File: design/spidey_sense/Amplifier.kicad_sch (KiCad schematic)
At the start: 5 parts, among them U6 LT1001

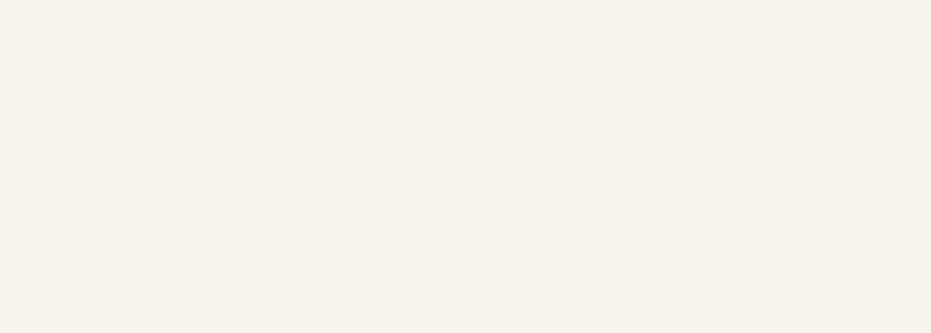
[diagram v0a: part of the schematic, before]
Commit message: Added vias to avoid GND loops
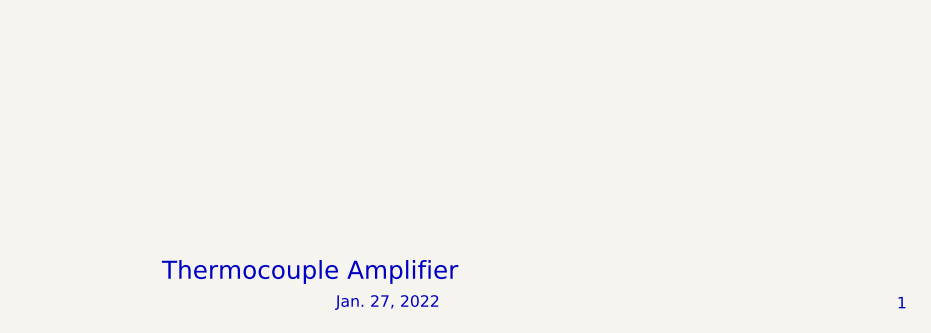
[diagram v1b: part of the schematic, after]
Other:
- note added: "1"
- note added: "Jan. 27, 2022"
- note added: "Thermocouple Amplifier"
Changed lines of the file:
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@@
     (stroke (width 0) (type default) (color 0 0 0 0))
+  )
+  (text "Thermocouple Amplifier" (at 186.6841 190.9188 0)
+    (effects (font (size 2 2)) (justify left bottom))
   )
   (text "R3*0.99 > 17.1k" (at 163.83 99.06 0)
@@
     (effects (font (size 1.27 1.27)) (justify left bottom))
   )
+  (text "1" (at 268.3346 194.1105 0)
+    (effects (font (size 1.27 1.27)) (justify left bottom))
+  )
+  (text "Jan. 27, 2022" (at 206.0014 193.9392 0)
+    (effects (font (size 1.27 1.27)) (justify left bottom))
+  )

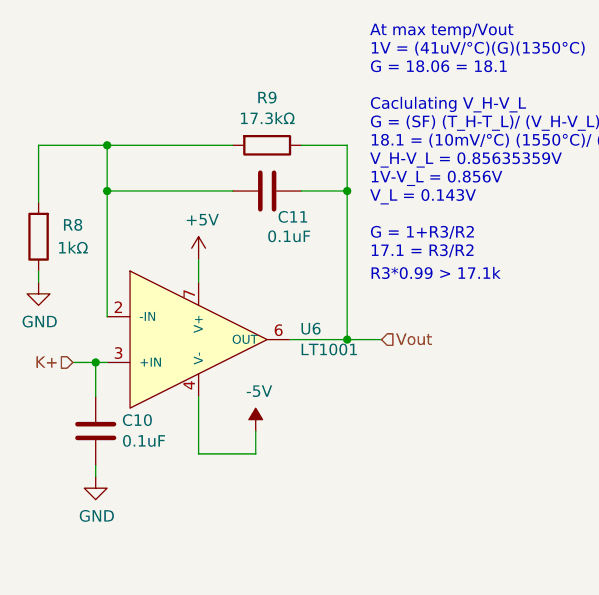
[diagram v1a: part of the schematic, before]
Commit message: Changed C5 value
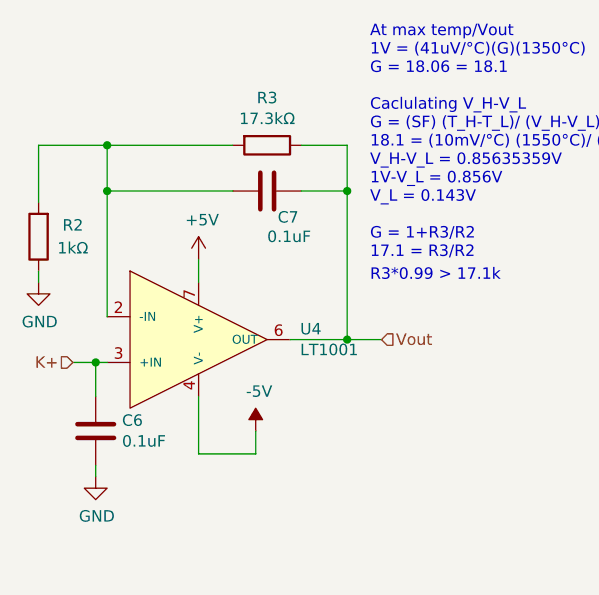
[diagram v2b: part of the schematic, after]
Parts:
- renumbered C10 to C6, C11 to C7, R8 to R2, R9 to R3, U6 to U4
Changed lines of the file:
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@@
   (symbol (lib_id "Device:R") (at 127 93.98 180)
     (in_bom yes) (on_board yes)
-    (property "Reference" "R8" (id 0) (at 130.81 92.71 0))
+    (property "Reference" "R2" (id 0) (at 130.81 92.71 0))
     (property "Value" "1kΩ" (id 1) (at 130.81 95.25 0))
     (property "Footprint" "Resistor_SMD:R_0805_2012Metric_Pad1.20x1.40mm_HandSolder" (id 2) (at 128.778 93.98 90)
@@
   (symbol (lib_id "Device:C") (at 133.35 115.57 0)
     (in_bom yes) (on_board yes)
-    (property "Reference" "C10" (id 0) (at 136.271 114.4016 0)
+    (property "Reference" "C6" (id 0) (at 136.271 114.4016 0)
       (effects (font (size 1.27 1.27)) (justify left))
     )
@@
   (symbol (lib_id "Device:C") (at 152.4 88.9 270)
     (in_bom yes) (on_board yes)
-    (property "Reference" "C11" (id 0) (at 153.5684 91.821 90)
+    (property "Reference" "C7" (id 0) (at 153.5684 91.821 90)
       (effects (font (size 1.27 1.27)) (justify left))
     )
@@
   (symbol (lib_id "power:GND") (at 133.35 120.65 0)
     (in_bom yes) (on_board yes)
-    (property "Reference" "#PWR026" (id 0) (at 133.35 127 0)
+    (property "Reference" "#PWR022" (id 0) (at 133.35 127 0)
       (effects (font (size 1.27 1.27)) hide)
     )
@@
   (symbol (lib_id "power:GND") (at 127 99.06 0)
     (in_bom yes) (on_board yes)
-    (property "Reference" "#PWR025" (id 0) (at 127 105.41 0)
+    (property "Reference" "#PWR021" (id 0) (at 127 105.41 0)
       (effects (font (size 1.27 1.27)) hide)
     )
@@
   (symbol (lib_id "Device:R") (at 152.4 83.82 270)
     (in_bom yes) (on_board yes)
-    (property "Reference" "R9" (id 0) (at 152.4 78.5622 90))
+    (property "Reference" "R3" (id 0) (at 152.4 78.5622 90))
     (property "Value" "17.3kΩ" (id 1) (at 152.4 80.8736 90))
     (property "Footprint" "Resistor_SMD:R_0805_2012Metric_Pad1.20x1.40mm_HandSolder" (id 2) (at 152.4 82.042 90)
@@
   (symbol (lib_id "power:+5V") (at 144.78 96.52 0)
     (in_bom yes) (on_board yes)
-    (property "Reference" "#PWR027" (id 0) (at 144.78 100.33 0)
+    (property "Reference" "#PWR023" (id 0) (at 144.78 100.33 0)
       (effects (font (size 1.27 1.27)) hide)
     )
@@
   (symbol (lib_id "power:-5V") (at 151.13 115.57 0)
     (in_bom yes) (on_board yes)
-    (property "Reference" "#PWR028" (id 0) (at 151.13 113.03 0)
+    (property "Reference" "#PWR024" (id 0) (at 151.13 113.03 0)
       (effects (font (size 1.27 1.27)) hide)
     )
@@
   (symbol (lib_id "Thermocouple:LT1001") (at 142.24 105.41 270)
     (in_bom yes) (on_board yes)
-    (property "Reference" "U6" (id 0) (at 156.0576 104.2416 90)
+    (property "Reference" "U4" (id 0) (at 156.0576 104.2416 90)
       (effects (font (size 1.27 1.27)) (justify left))
     )
